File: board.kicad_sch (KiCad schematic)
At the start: 115 parts, among them J1 Conn_01x04, J10 878311420, J2 Conn_2Rows-33Pins, J3 Conn_2Rows-33Pins, J4 Conn_2Rows-33Pins, J5 Conn_2Rows-33Pins, J6 Conn_2Rows-33Pins, J7 Conn_2Rows-33Pins, J8 Conn_01x04, J9 Conn_01x04, U1 MC68060RC50, U10 74LVC162245ADGG, U11 74LVC162245ADGG, U12 SIT2001BI-S2-33E-50.000000G, U13 74LVC162245ADGG, U14 SC16IS762IPW, U15 CH9350, U16 AP2161W, U17 AP2161W, U2 LCMXO2-7000HC-6TG144I, U3 SST39VF1601C-70-4C-EKE, U4 IS61WV51216BLL-10TLI, U5 IS61WV51216BLL-10TLI, U6 SST39VF1601C-70-4C-EKE, U7 74LVC162245ADGG, U8 74LVC162245ADGG, U9 74LVC162245ADGG, Y1 1.8432 MHz

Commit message: Reset and CPLD decoupling added
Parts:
- added J11: Conn_01x02, Connector_PinHeader_1.00mm:PinHeader_1x02_P1.00mm_Vertical, symbol Connector_Generic:Conn_01x02
- added R1: 10kR, Resistor_SMD:R_0805_2012Metric_Pad1.20x1.40mm_HandSolder, symbol Device:R
- added R17: 50kR, Resistor_SMD:R_0805_2012Metric_Pad1.20x1.40mm_HandSolder, symbol Device:R
- added U18: TPS3808DBV, Package_TO_SOT_SMD:SOT-23-6, symbol Power_Supervisor:TPS3808DBV
- added U19: PCA9515AD, i2c_buffer:SOT96-1_NXP, symbol i2c_buffer:PCA9515AD
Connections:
- net EXT_PA-CLK: now also J6.8 (Pin_8); no longer J6.2 (Pin_2)
- net EXT_PA-CLKEN: now also J6.10 (Pin_10); no longer J6.4 (Pin_4)
- net EXT_PA-SPI-CS-LATCH: now also J6.16 (Pin_16); no longer J6.10 (Pin_10)
- net EXT_PA-SPI-MOSI: now also J6.14 (Pin_14); no longer J6.8 (Pin_8)
- net EXT_PA-SPI-SCLK: now also J6.12 (Pin_12); no longer J6.6 (Pin_6)
- net GND: now also J11.1 (Pin_1), U18.2 (GND), U19.4 (GND)
- net I2C-MCLK: now also U19.2 (SCL0)
- net I2C-MDATA: now also U19.3 (SDA0)
- net U1B-RSTI: now also R1.2, U18.1 (~{RESET}); no longer U2.96 (PR9A)
- net VCC: now also R1.1, R17.1, U18.5 (SENSE), U18.6 (VDD), U19.8 (VCC)
- net EXT_PA0: no longer names the net of U11.9 (1B5)
- net EXT_PA0: no longer J6.12 (Pin_12)
- net EXT_PA1: no longer names the net of U11.11 (1B6)
- net EXT_PA1: no longer J6.14 (Pin_14)
- net PA0: no longer names the net of U11.40 (1A5)
- net PA1: no longer names the net of U11.38 (1A6)
- new net: J11.2 (Pin_2), U18.3 (~{MR})
- new net: R17.2, U18.4 (CT)
- new net EXT_I2C-MCLK: J6.6 (Pin_6), U19.7 (SCL2)
- new net EXT_I2C-MDATA: J6.4 (Pin_4), U19.6 (SDA1)

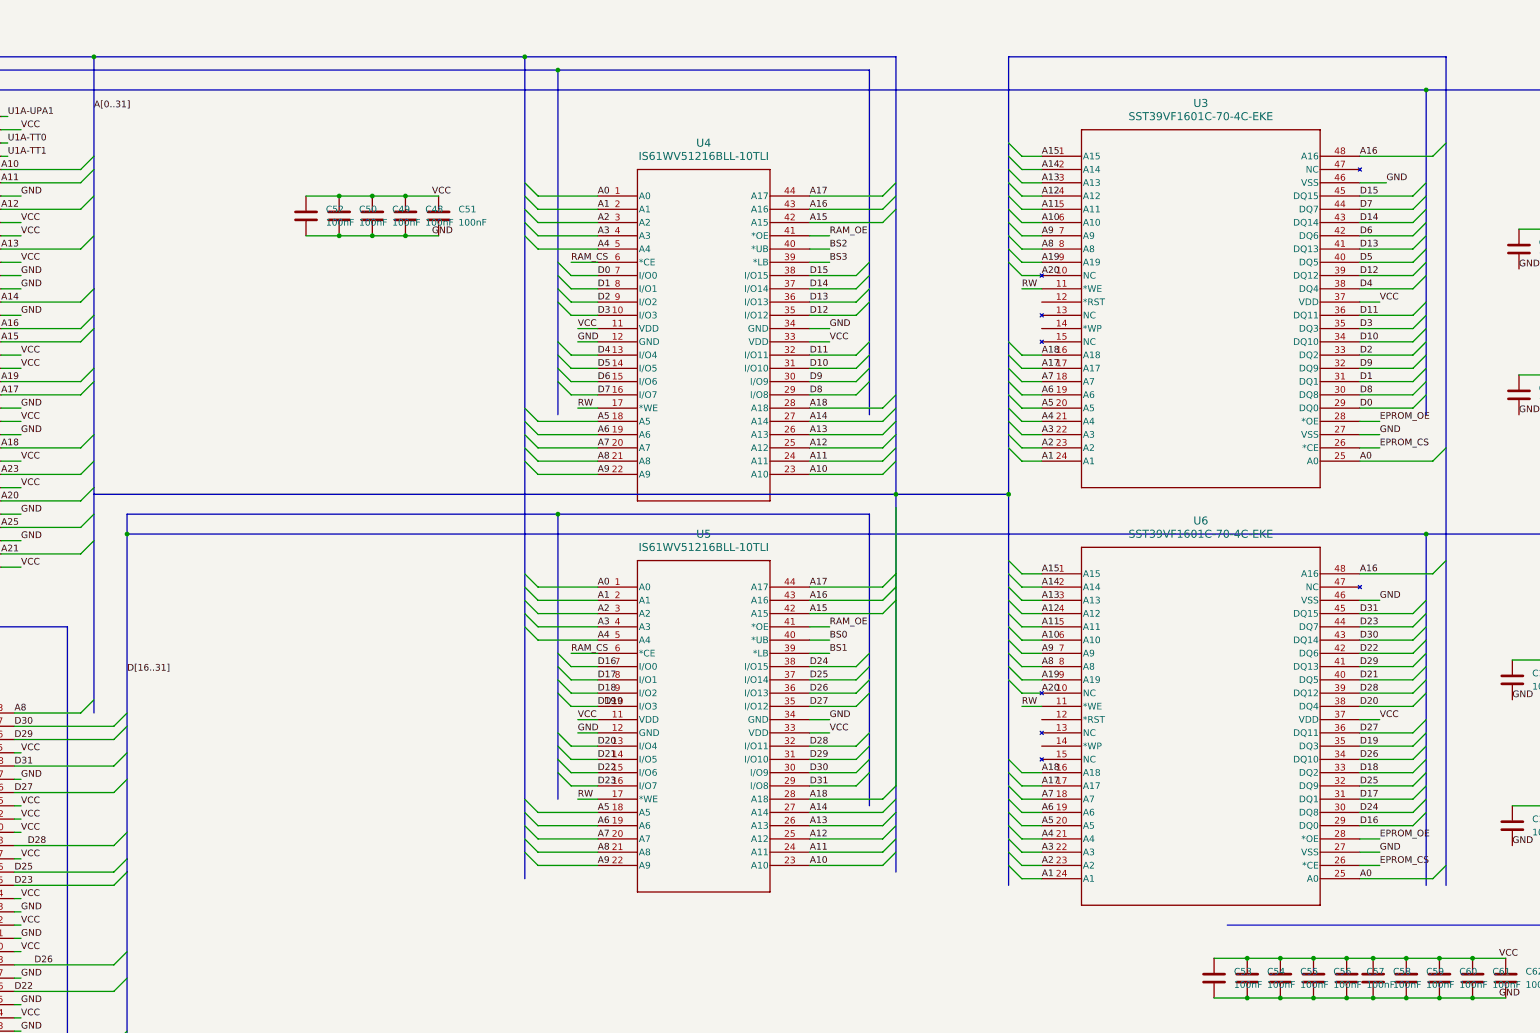
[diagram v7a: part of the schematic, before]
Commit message: Buses re-wired
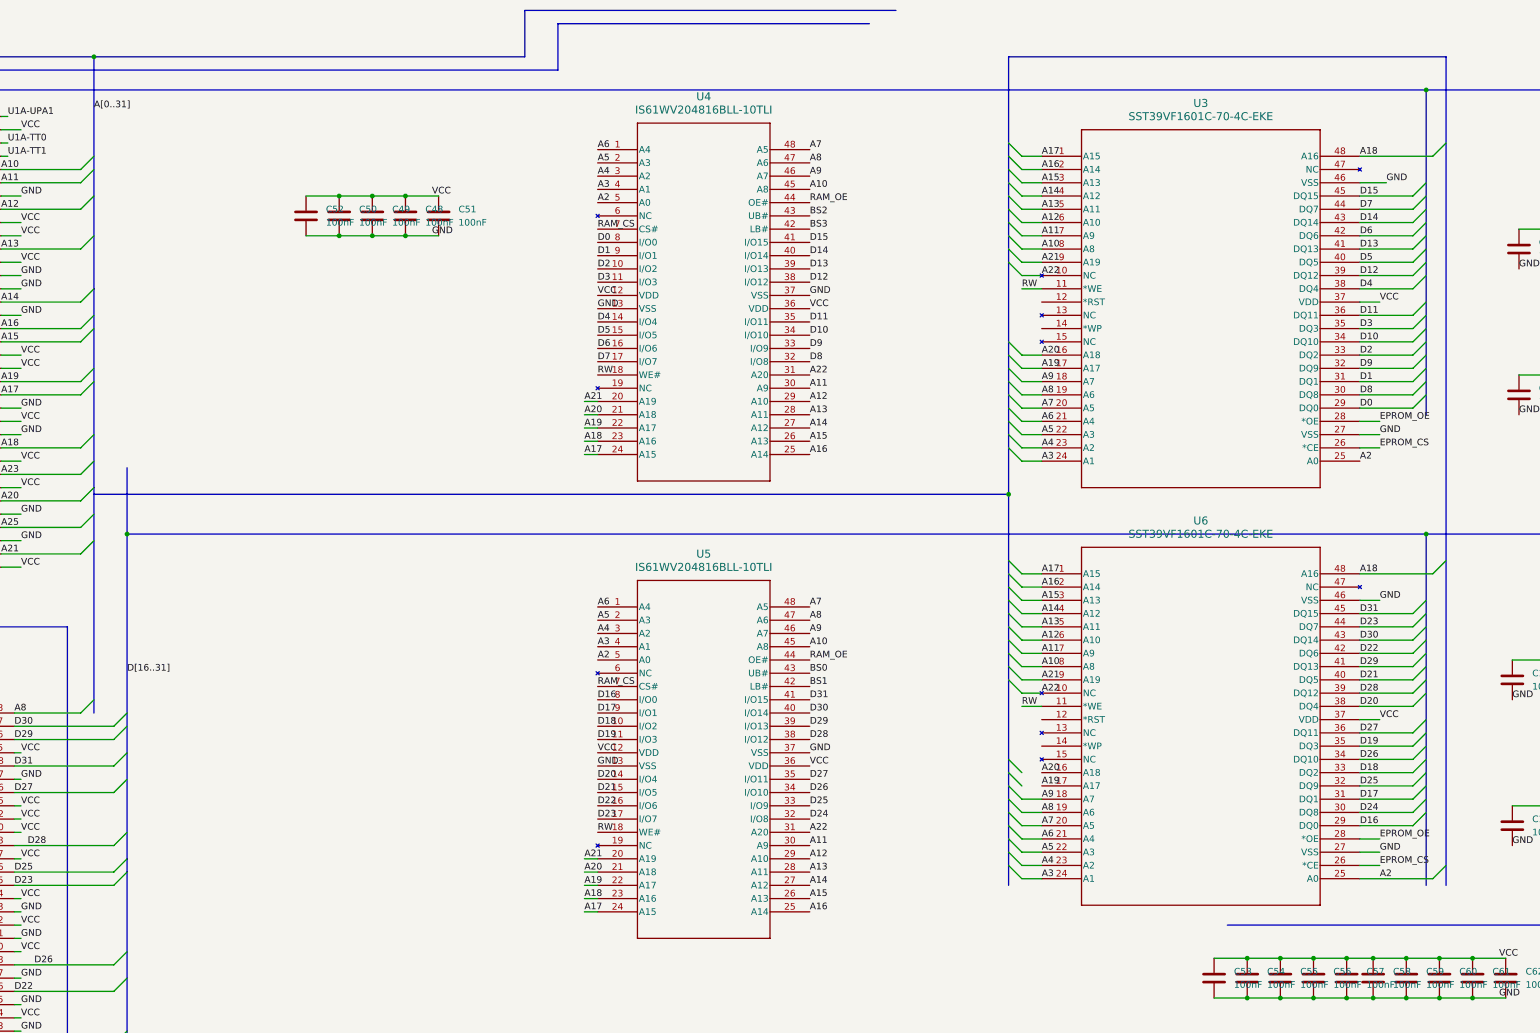
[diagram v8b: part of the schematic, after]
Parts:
- removed U5: IS61WV51216BLL-10TLI, sram:TSOP-2_44L_400MIL_ISI, symbol SRAM:IS61WV51216BLL-10TLI
- added U5: IS61WV204816BLL-10TLI, new_sram:48L_TSOP-1_12X20_ISI, symbol new_sram:IS61WV204816BLL-10TLI
- U3, U6: footprint flash:TSOP48_EKE_SST_MCH -> TSOP48_EKE_SST_MCH
- U4: value IS61WV51216BLL-10TLI -> IS61WV204816BLL-10TLI; footprint sram:TSOP-2_44L_400MIL_ISI -> new_sram:48L_TSOP-1_12X20_ISI; symbol SRAM:IS61WV51216BLL-10TLI -> new_sram:IS61WV204816BLL-10TLI
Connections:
- net A0: no longer U3.25 (A0), U4.1 (A0), U6.25 (A0)
- net A1: no longer U3.24 (A1), U4.2 (A1), U6.24 (A1)
- net A10: now also U3.8 (A8), U4.45 (A8), U6.8 (A8), U5.45 (A8); no longer U3.6 (A10), U4.23 (A10), U6.6 (A10)
- net A11: now also U3.7 (A9), U4.30 (A9), U6.7 (A9), U5.30 (A9); no longer U3.5 (A11), U4.24 (A11), U6.5 (A11)
- net A12: now also U3.6 (A10), U4.29 (A10), U6.6 (A10), U5.29 (A10); no longer U3.4 (A12), U4.25 (A12), U6.4 (A12)
- net A13: now also U3.5 (A11), U4.28 (A11), U6.5 (A11), U5.28 (A11); no longer U3.3 (A13), U4.26 (A13), U6.3 (A13)
- net A14: now also U3.4 (A12), U6.4 (A12), U5.27 (A12); no longer U3.2 (A14), U6.2 (A14)
- net A15: now also U3.3 (A13), U4.26 (A13), U6.3 (A13), U5.26 (A13); no longer U3.1 (A15), U4.42 (A15), U6.1 (A15)
- net A16: now also U3.2 (A14), U4.25 (A14), U6.2 (A14), U5.25 (A14); no longer U3.48 (A16), U4.43 (A16), U6.48 (A16)
- net A17: now also U3.1 (A15), U4.24 (A15), U6.1 (A15), U5.24 (A15); no longer U3.17 (A17), U4.44 (A17), U6.17 (A17)
- net A18: now also U3.48 (A16), U4.23 (A16), U6.48 (A16), U5.23 (A16); no longer U3.16 (A18), U4.28 (A18), U6.16 (A18)
- net A19: now also U3.17 (A17), U4.22 (A17), U6.17 (A17), U5.22 (A17); no longer U3.9 (A19), U6.9 (A19)
- net A2: now also U3.25 (A0), U4.5 (A0), U6.25 (A0), U5.5 (A0); no longer U3.23 (A2), U4.3 (A2), U6.23 (A2)
- net A20: now also U3.16 (A18), U4.21 (A18), U6.16 (A18), U5.21 (A18); no longer U3.10 (NC), U6.10 (NC)
- net A21: now also U3.9 (A19), U4.20 (A19), U6.9 (A19), U5.20 (A19)
- net A22: now also U3.10 (NC), U4.31 (A20), U6.10 (NC), U5.31 (A20)
- net A3: now also U3.24 (A1), U6.24 (A1), U5.4 (A1); no longer U3.22 (A3), U6.22 (A3)
- net A4: now also U3.23 (A2), U4.3 (A2), U6.23 (A2), U5.3 (A2); no longer U3.21 (A4), U4.5 (A4), U6.21 (A4)
- net A5: now also U3.22 (A3), U4.2 (A3), U6.22 (A3), U5.2 (A3); no longer U3.20 (A5), U4.18 (A5), U6.20 (A5)
- net A6: now also U3.21 (A4), U4.1 (A4), U6.21 (A4), U5.1 (A4); no longer U3.19 (A6), U4.19 (A6), U6.19 (A6)
- net A7: now also U3.20 (A5), U4.48 (A5), U6.20 (A5), U5.48 (A5); no longer U3.18 (A7), U4.20 (A7), U6.18 (A7)
- net A8: now also U3.19 (A6), U4.47 (A6), U6.19 (A6), U5.47 (A6); no longer U3.8 (A8), U4.21 (A8), U6.8 (A8)
- net A9: now also U3.18 (A7), U4.46 (A7), U6.18 (A7), U5.46 (A7); no longer U3.7 (A9), U4.22 (A9), U6.7 (A9)
- net BS0: now also U5.43 (UB#)
- net BS1: now also U5.42 (LB#)
- net BS2: now also U4.43 (UB#); no longer U4.40 (*UB)
- net BS3: now also U4.42 (LB#); no longer U4.39 (*LB)
- net D0: now also U4.8 (I/O0); no longer U4.7 (I/O0)
- net D1: now also U4.9 (I/O1); no longer U4.8 (I/O1)
- net D10: now also U4.34 (I/O10); no longer U4.31 (I/O10)
- net D11: now also U4.35 (I/O11); no longer U4.32 (I/O11)
- net D12: now also U4.38 (I/O12); no longer U4.35 (I/O12)
- net D13: now also U4.39 (I/O13); no longer U4.36 (I/O13)
- net D14: now also U4.40 (I/O14); no longer U4.37 (I/O14)
- net D15: now also U4.41 (I/O15); no longer U4.38 (I/O15)
- net D16: now also U5.8 (I/O0)
- net D17: now also U5.9 (I/O1)
- net D18: now also U5.10 (I/O2)
- net D19: now also U5.11 (I/O3)
- net D2: now also U4.10 (I/O2); no longer U4.9 (I/O2)
- net D20: now also U5.14 (I/O4)
- net D21: now also U5.15 (I/O5)
- net D22: now also U5.16 (I/O6)
- net D23: now also U5.17 (I/O7)
- net D24: now also U5.32 (I/O8)
- net D25: now also U5.33 (I/O9)
- net D26: now also U5.34 (I/O10)
- net D27: now also U5.35 (I/O11)
- net D28: now also U5.38 (I/O12)
- net D29: now also U5.39 (I/O13)
- net D3: now also U4.11 (I/O3); no longer U4.10 (I/O3)
- net D30: now also U5.40 (I/O14)
- net D31: now also U5.41 (I/O15)
- net D4: now also U4.14 (I/O4); no longer U4.13 (I/O4)
- net D5: now also U4.15 (I/O5); no longer U4.14 (I/O5)
- net D6: now also U4.16 (I/O6); no longer U4.15 (I/O6)
- net D7: now also U4.17 (I/O7); no longer U4.16 (I/O7)
- net D8: now also U4.32 (I/O8); no longer U4.29 (I/O8)
- net D9: now also U4.33 (I/O9); no longer U4.30 (I/O9)
- net GND: now also U4.13 (VSS), U4.37 (VSS), U5.13 (VSS), U5.37 (VSS); no longer U4.12 (GND), U4.34 (GND)
- net RAM_CS: now also U4.7 (CS#), U5.7 (CS#); no longer U4.6 (*CE)
- net RAM_OE: now also U4.44 (OE#), U5.44 (OE#); no longer U4.41 (*OE)
- net RW: now also U4.18 (WE#), U5.18 (WE#); no longer U4.17 (*WE)
- net VCC: now also U4.12 (VDD), U4.36 (VDD), U5.12 (VDD), U5.36 (VDD); no longer U4.11 (VDD), U4.33 (VDD)
